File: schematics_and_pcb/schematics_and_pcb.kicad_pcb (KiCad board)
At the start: 2 copper layers, 82.2 x 89.8 mm, 84 parts, among them J1 RND 205-00623, J2 RND 205-00627, J3 Motor con, J4 Conn_01x04_Male, J5 Conn_01x04_Male, Q1 PMV213SN, SW1 RND 210-00210, U1 MIC5235YM5-TR, U2 AP2125N-3.3TRG1, U3 PWM3389DM-T3QU, U4 STM32F401RBTx, Y1 YLFXTAL029370

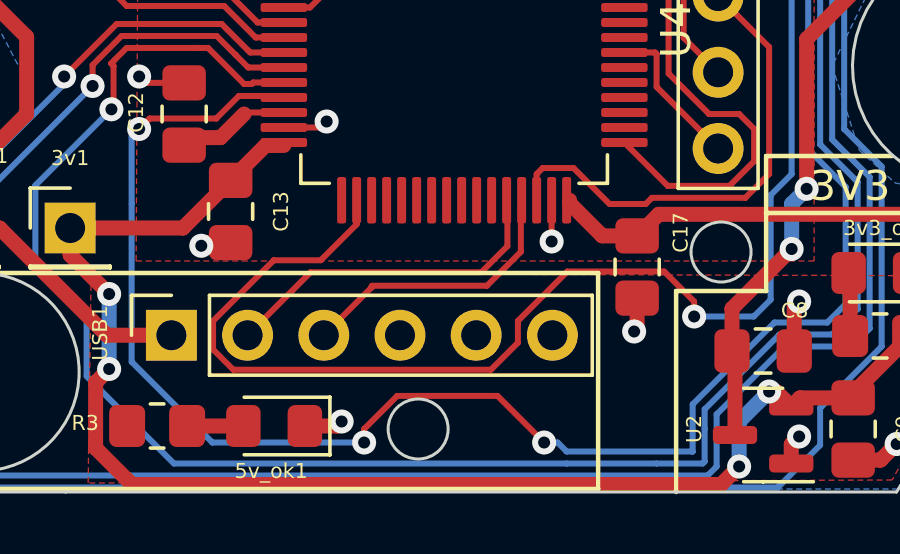
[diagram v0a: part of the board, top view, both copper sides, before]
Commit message: added a logo
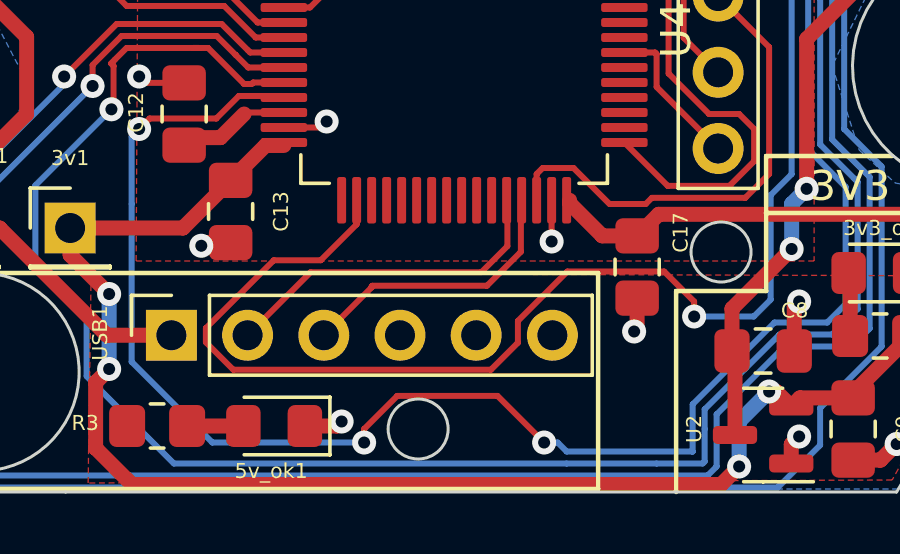
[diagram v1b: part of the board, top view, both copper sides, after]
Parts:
- added G***: LOGO, LOGO, B.Cu at (44.2, 87.9)
- added G***: LOGO, LOGO, B.Cu at (98.0, 68.7)
- added G***: LOGO, LOGO, B.Cu at (98.0, 87.2)
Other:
- board text added: "Mouse Logo Vectors by Vecteezy"
- board text removed: "BRIDGING THE GAP IN GND"

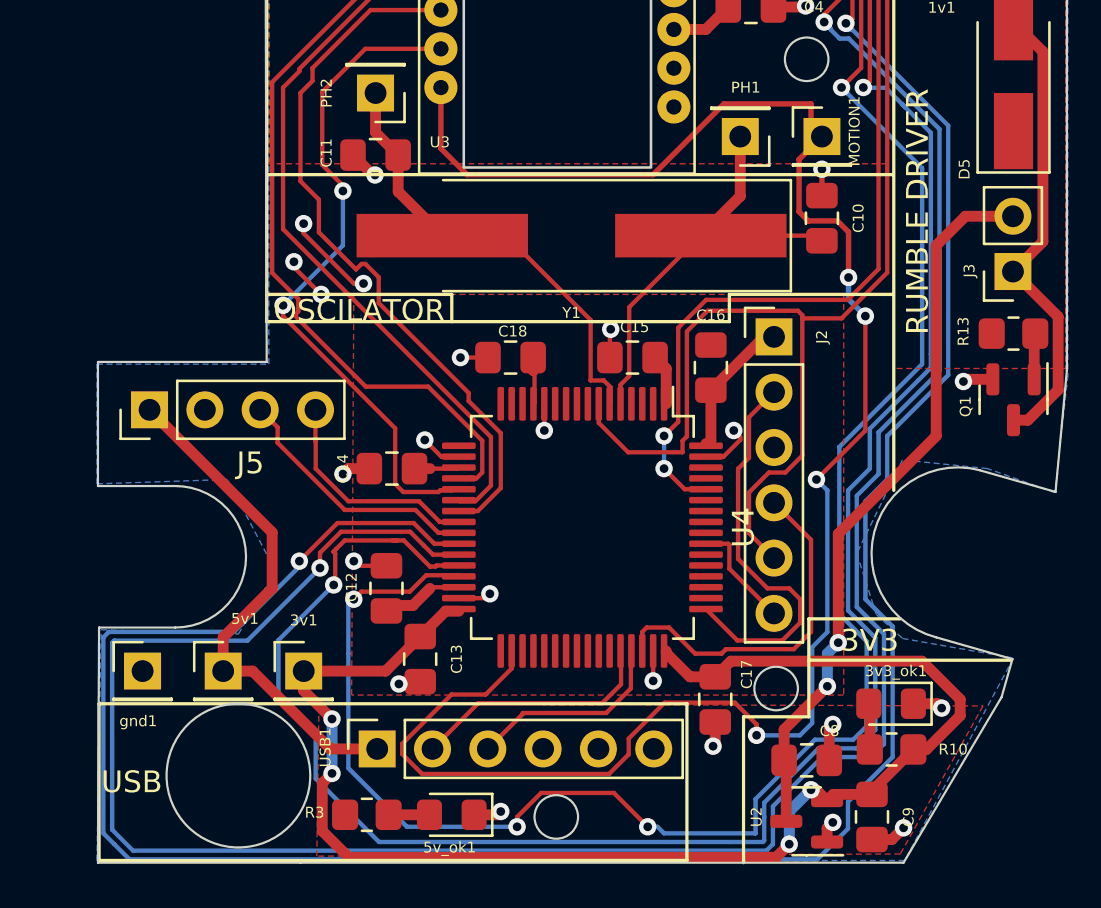
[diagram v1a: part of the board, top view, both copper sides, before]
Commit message: added pin for the rumble
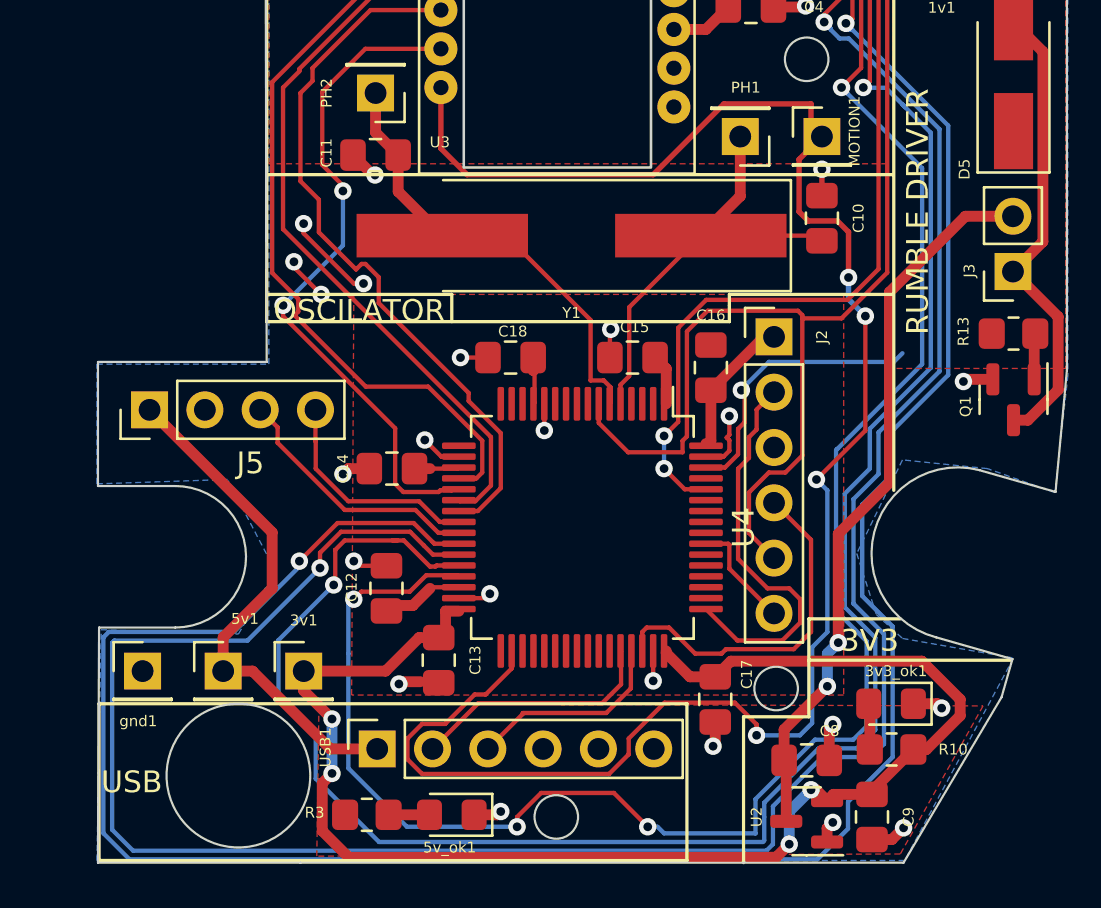
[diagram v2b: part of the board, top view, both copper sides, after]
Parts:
- moved C13 0.85 mm to (37.9, 94.8)
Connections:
- U4 pad 62: unconnected-(U4-Pad62) -> RUMBLE
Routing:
- net RUMBLE: track 0.00 -> 13.0 mm, vias 0 -> 1
- net VDDIO: track 127.4 -> 127.9 mm

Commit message: moved lib
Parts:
- moved R13 0.57 mm to (64.7, 79.4)
- moved Q1 0.53 mm to (64.6, 82.4)
- moved J3 0.50 mm to (64.6, 76.5)
- moved D5 0.42 mm to (64.6, 67.7)
- moved 1v1 0.32 mm to (60.7, 62.4)
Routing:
- net RUMBLE: track 13.0 -> 17.9 mm, vias 1 -> 2
- net +5V: track 78.5 -> 82.8 mm
- net VDD: track 39.5 -> 36.6 mm
- net SPI2_MISO: track 33.6 -> 36.1 mm
- net Net-(D5-Pad2): track 21.5 -> 19.4 mm
- net PHASE_B: track 138.0 -> 139.5 mm
- net SPI2_MOSI: track 33.3 -> 34.6 mm
- net RIGHT_STATE: track 147.0 -> 147.9 mm
- net NRST: track 75.8 -> 76.5 mm
- net LEFT_STATE: track 178.6 -> 179.3 mm
- net PHASE_A: track 146.5 -> 147.1 mm
- net GND: track 63.1 -> 63.8 mm

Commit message: some fixes
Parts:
- removed LED1, LED10, LED11, LED12, LED2, LED3, LED4, LED5, LED6, LED7, LED8, LED9: RND_135-00249, mouse:RND_135-00249
- moved C14 1.10 mm to (35.8, 84.9), turned to 90 degrees
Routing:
- net VDD: track 36.6 -> 39.6 mm
- net VDDIO: track 127.9 -> 128.9 mm
- net SPI2_NCS: track 36.4 -> 35.5 mm
- net SPI2_SCK: track 31.1 -> 31.9 mm
- net SPI2_MISO: track 36.1 -> 35.3 mm
- net FRONT_STATE: track 35.2 -> 35.7 mm
- net BACK_STATE: track 31.2 -> 31.7 mm
- net GND: track 63.8 -> 64.1 mm, vias 39 -> 38

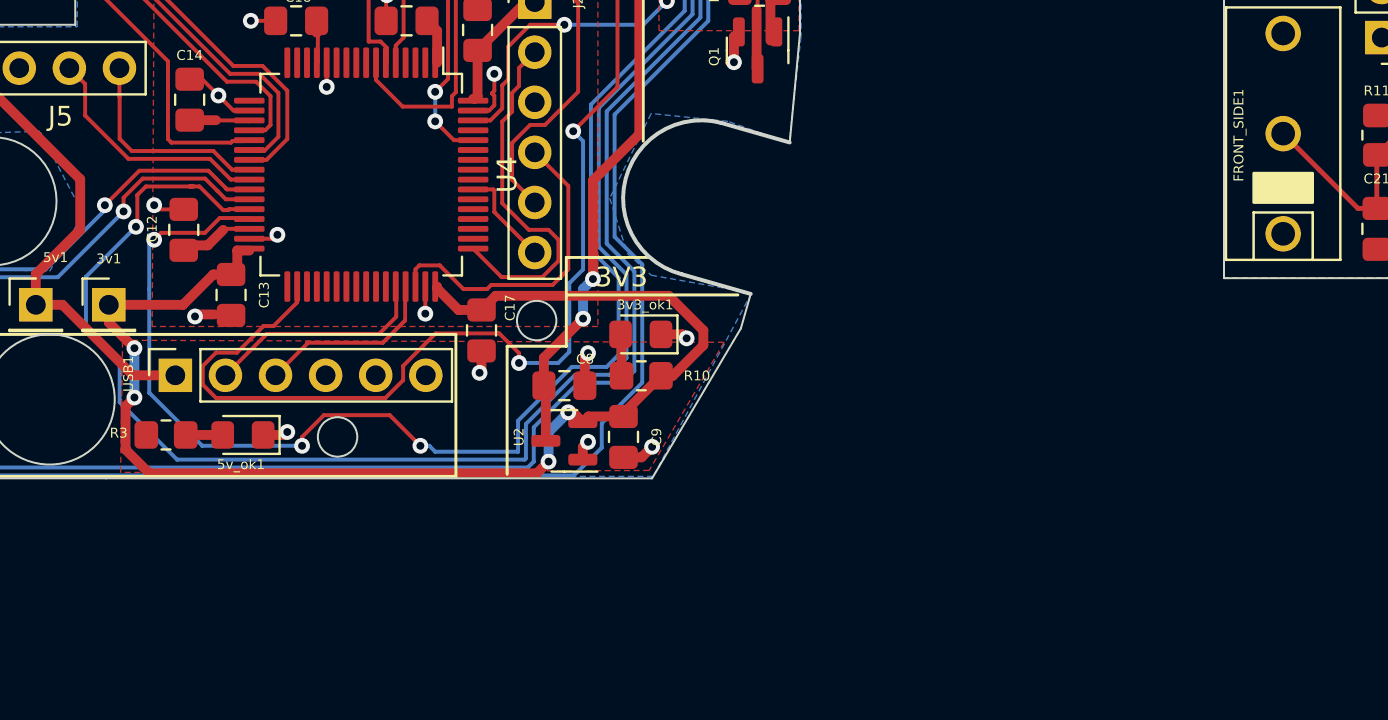
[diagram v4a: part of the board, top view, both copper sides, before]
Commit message: changed to custom usb connector with only 4 pins.
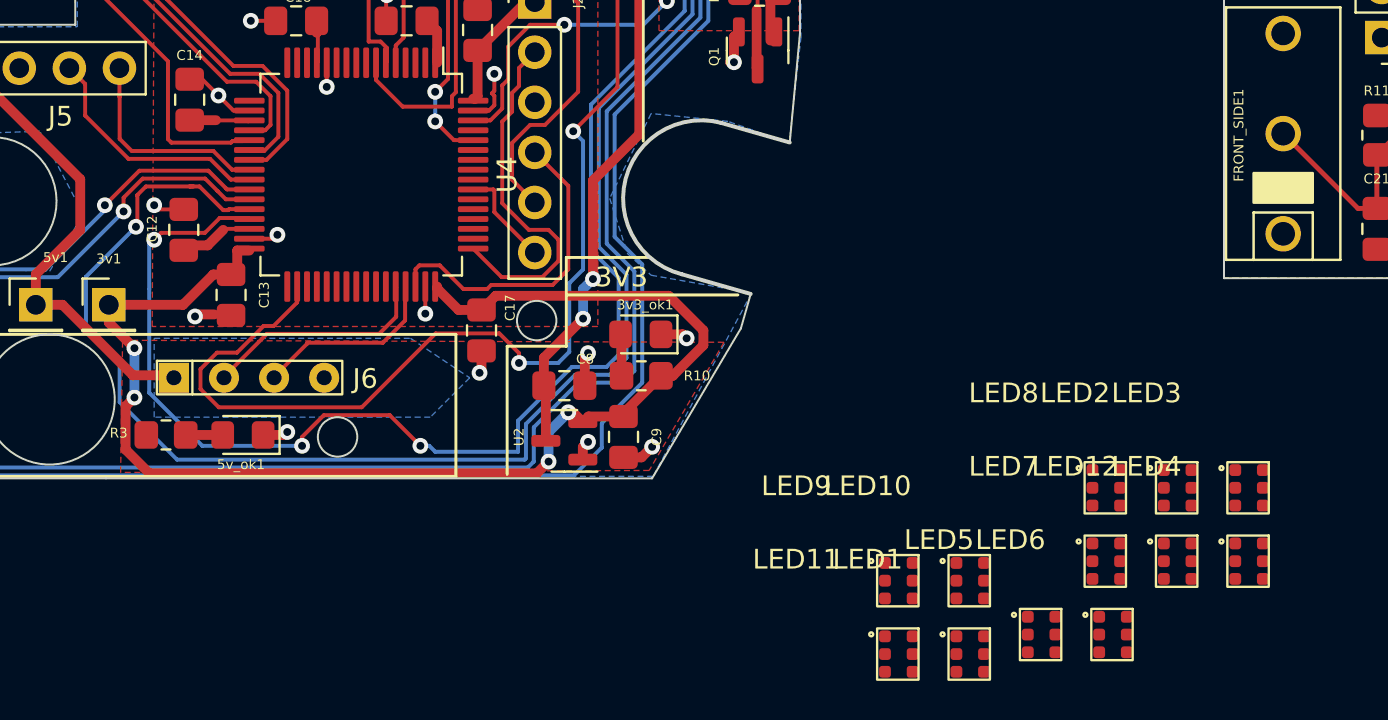
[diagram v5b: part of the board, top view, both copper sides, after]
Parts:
- removed USB1: USB_OTG, Connector_PinSocket_2.54mm:PinSocket_1x06_P2.54mm_Vertical
- added J6: USB_OTG_custom, mouse:USB_2.45, F.Cu at (37.5, 101.5)
- added LED1: RND_135-00249, mouse:RND_135-00249, F.Cu at (75.4, 113.0)
- added LED10: RND_135-00249, mouse:RND_135-00249, F.Cu at (75.4, 109.3)
- added LED11: RND_135-00249, mouse:RND_135-00249, F.Cu at (71.8, 113.0)
- added LED12: RND_135-00249, mouse:RND_135-00249, F.Cu at (85.9, 108.3)
- added LED2: RND_135-00249, mouse:RND_135-00249, F.Cu at (85.9, 104.6)
- added LED3: RND_135-00249, mouse:RND_135-00249, F.Cu at (89.5, 104.6)
- added LED4: RND_135-00249, mouse:RND_135-00249, F.Cu at (89.5, 108.3)
- added LED5: RND_135-00249, mouse:RND_135-00249, F.Cu at (79.0, 112.0)
- added LED6: RND_135-00249, mouse:RND_135-00249, F.Cu at (82.6, 112.0)
- added LED7: RND_135-00249, mouse:RND_135-00249, F.Cu at (82.3, 108.3)
- added LED8: RND_135-00249, mouse:RND_135-00249, F.Cu at (82.3, 104.6)
- added LED9: RND_135-00249, mouse:RND_135-00249, F.Cu at (71.8, 109.3)

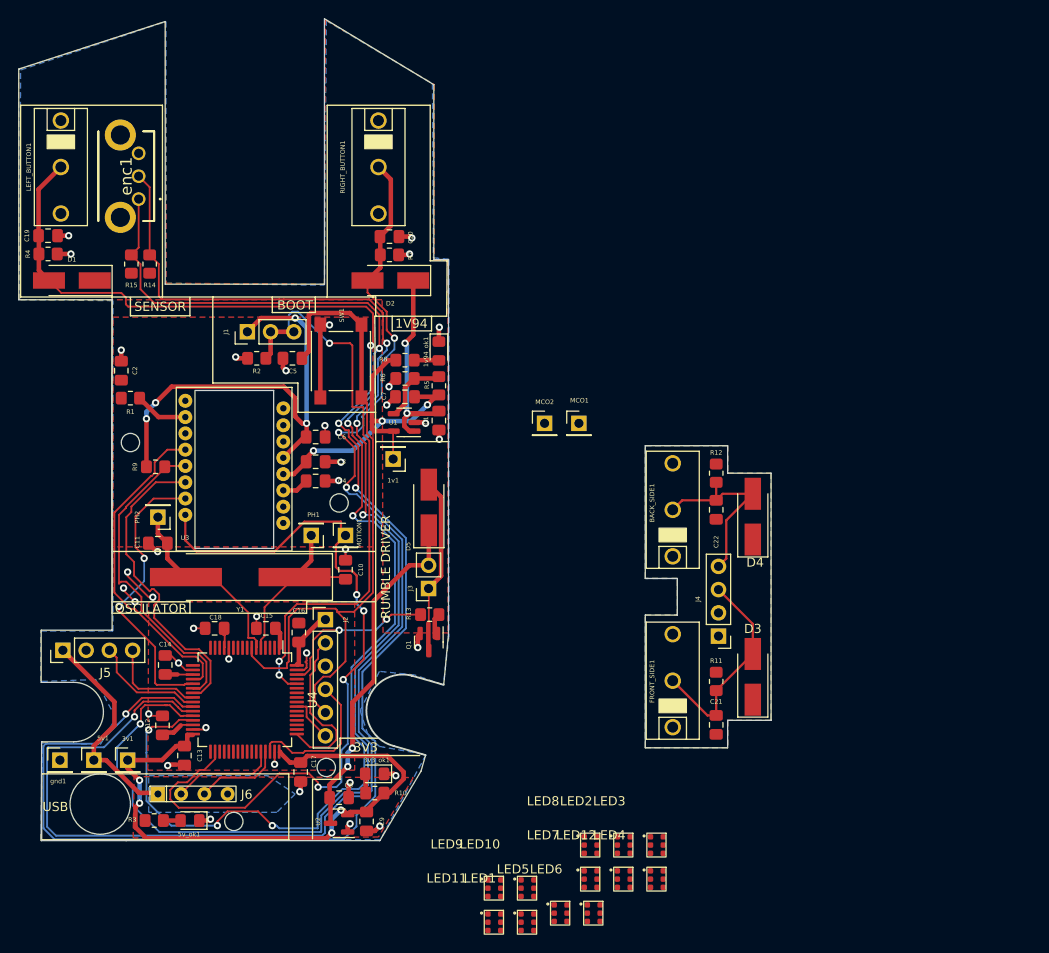
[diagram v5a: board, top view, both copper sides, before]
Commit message: fixed some drc issues
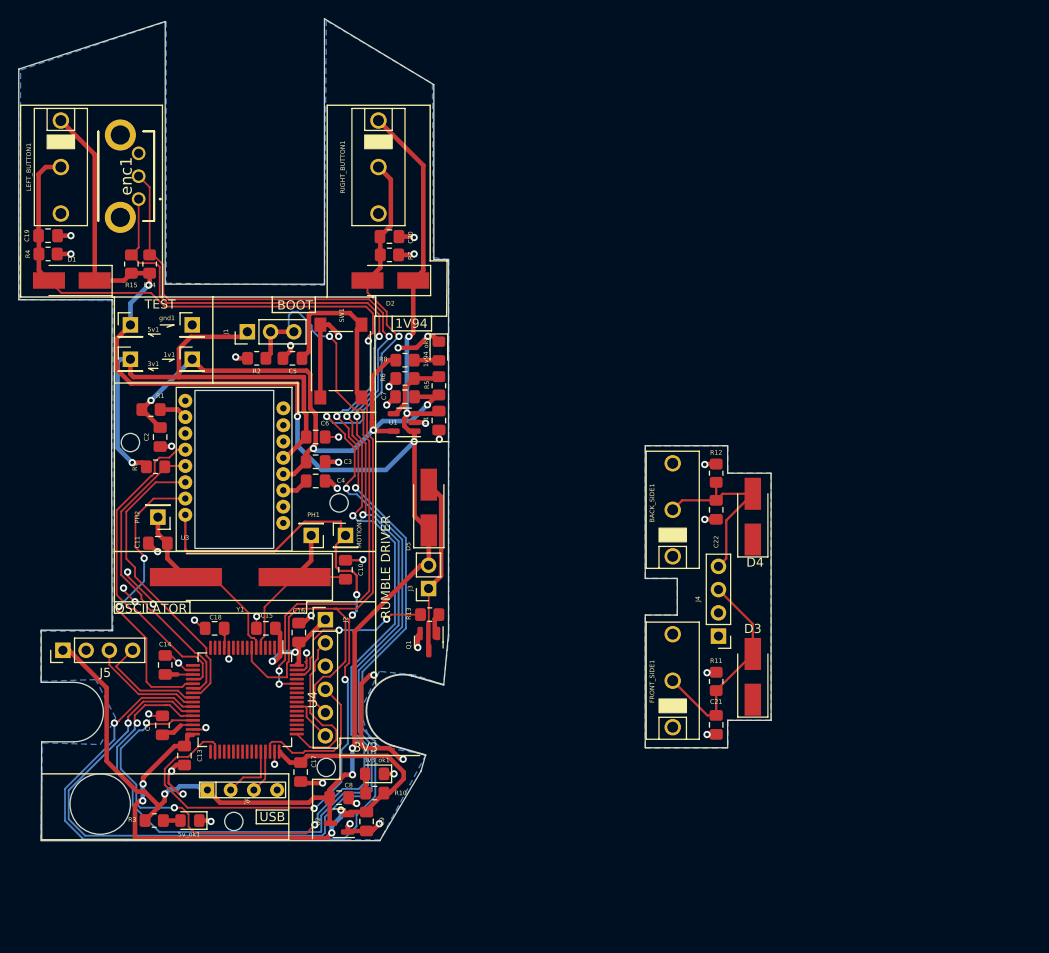
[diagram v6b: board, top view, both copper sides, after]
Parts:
- removed LED1, LED10, LED11, LED12, LED2, LED3, LED4, LED5, LED6, LED7, LED8, LED9: RND_135-00249, mouse:RND_135-00249
- removed MCO1: MCO1_TEST, Connector_PinHeader_2.54mm:PinHeader_1x01_P2.54mm_Vertical
- removed MCO2: MCO2_TEST, Connector_PinHeader_2.54mm:PinHeader_1x01_P2.54mm_Vertical
- moved gnd1 49.7 mm to (38.8, 47.8)
- moved 5v1 47.7 mm to (32.0, 47.8)
- moved 3v1 43.8 mm to (32.0, 51.5)
- moved 1v1 24.5 mm to (38.8, 51.5), turned to 0 degrees
- moved C2 8.40 mm to (35.2, 60.0), turned to -90 degrees
- moved J6 5.43 mm to (43.0, 101.1)
- moved R1 2.57 mm to (34.2, 57.0)
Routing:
- net +5V: track 82.8 -> 216.5 mm, vias 4 -> 8
- net GND: track 64.1 -> 98.2 mm, vias 38 -> 47
- net VDD: track 39.6 -> 69.4 mm, vias 3 -> 4
- net VDDIO: track 128.9 -> 139.8 mm, vias 8 -> 7
- net LEFT_STATE: track 179.3 -> 173.4 mm
- net D+: track 9.47 -> 4.71 mm
- net D-: track 11.4 -> 6.68 mm
- net PHASE_B: track 139.7 -> 144.0 mm
- net RIGHT_STATE: track 147.9 -> 143.9 mm
- net LEDP: track 5.86 -> 3.09 mm
- net NRST: track 76.5 -> 79.0 mm
- net SPI2_MOSI: track 34.6 -> 32.7 mm
- net MOTION: track 84.1 -> 85.7 mm
- net SPI2_MISO: track 35.3 -> 33.7 mm
- net BACK_STATE: track 31.7 -> 33.3 mm
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- removed copper zone on F.Cu, net VDD
- removed copper zone on F.Cu, net VDDIO
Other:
- board text added: "TEST"
- board text removed: "SENSOR"

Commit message: filled out the readme
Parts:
- removed BACK_SIDE1, FRONT_SIDE1: D2F-01F, mouse:D2F-01F
- removed C21, C22: 10u, Capacitor_SMD:C_0805_2012Metric_Pad1.18x1.45mm_HandSolder
- removed D1, D3, D4: S1A, Diode_SMD:D_SMA_Handsoldering
- removed D2: 1N4001, Diode_SMD:D_SMA_Handsoldering
- removed the G*** at (98.0, 68.7)
- removed the G*** at (98.0, 87.2)
- removed J4: Conn_01x04_Male, Connector_PinHeader_2.54mm:PinHeader_1x04_P2.54mm_Vertical
- removed R11, R12: 4.7k, Resistor_SMD:R_0805_2012Metric_Pad1.20x1.40mm_HandSolder
- removed R5: 10k, Resistor_SMD:R_0805_2012Metric_Pad1.20x1.40mm_HandSolder
- removed R6: 18k, Resistor_SMD:R_0805_2012Metric_Pad1.20x1.40mm_HandSolder
- added C23: 4u7, Capacitor_SMD:C_0805_2012Metric_Pad1.18x1.45mm_HandSolder, F.Cu at (62.0, 55.6)
- U1: value MIC5235YM5-TR -> LP2985IM5-2.0/NOPB
- U2: value AP2125N-3.3TRG1 -> TS3480CX33 RFG
- moved R8 4.56 mm to (65.6, 54.4), turned to 90 degrees
- moved 1v94_ok1 3.83 mm to (62.0, 51.6), turned to 0 degrees
- moved C7 2.00 mm to (62.0, 53.6)
- turned C9 to 90 degrees
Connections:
- C18 pad 2: GND -> VDDIO
- U2 pad 1: GND -> VDDIO
- U2 pad 2: VDDIO -> +5V
- U2 pad 3: +5V -> GND
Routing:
- net VDDIO: track 139.8 -> 211.9 mm, vias 7 -> 11
- net FRONT_STATE: track 35.7 -> 12.4 mm
- net BACK_STATE: track 33.3 -> 10.8 mm
- net VDD: track 69.4 -> 60.6 mm
- net GND: track 98.2 -> 105.8 mm, vias 47 -> 44
- net Net-(U1-Pad4): track 7.65 -> 2.09 mm
- net +5V: track 216.5 -> 212.5 mm
- net LEFT_STATE: track 173.4 -> 175.7 mm
- net MOTION: track 85.7 -> 84.4 mm
- net Net-(1v94_ok1-Pad2): track 2.71 -> 3.67 mm
- net PHASE_B: track 144.0 -> 144.7 mm
- net PHASE_A: track 147.3 -> 147.9 mm
- net SPI2_MISO: track 33.7 -> 34.3 mm
- removed copper zone on F.Cu, net +5V
- removed copper zone on B.Cu, net GND
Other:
- board size 82.2 x 89.8 mm -> 47 x 89.8 mm
- board text added: "1v8"
- board text added: "Awesome gaming mouse"
- board text added: "CLK"
- board text added: "D+"
- board text added: "D-"
- board text added: "GND"
- board text added: "IO"
- board text added: "RST"
- board text added: "SIDE BUTTON HEADER"
- board text added: "SWO"
- board text added: "VCC"
- board text added: "VDD"
- board text removed: "1V94"
- board text removed: "EPICLY PRO GAMER MOUSE"
- board text removed: "MOUSEWHEEL STUFF"
- board text removed: "SIDE BUTTONS"
